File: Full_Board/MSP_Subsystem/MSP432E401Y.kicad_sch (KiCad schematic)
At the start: 4 parts, among them J1-J2 Conn_01x10, J3-J4 Conn_01x10, J5-J6 Conn_01x10, J7-J8 Conn_01x10

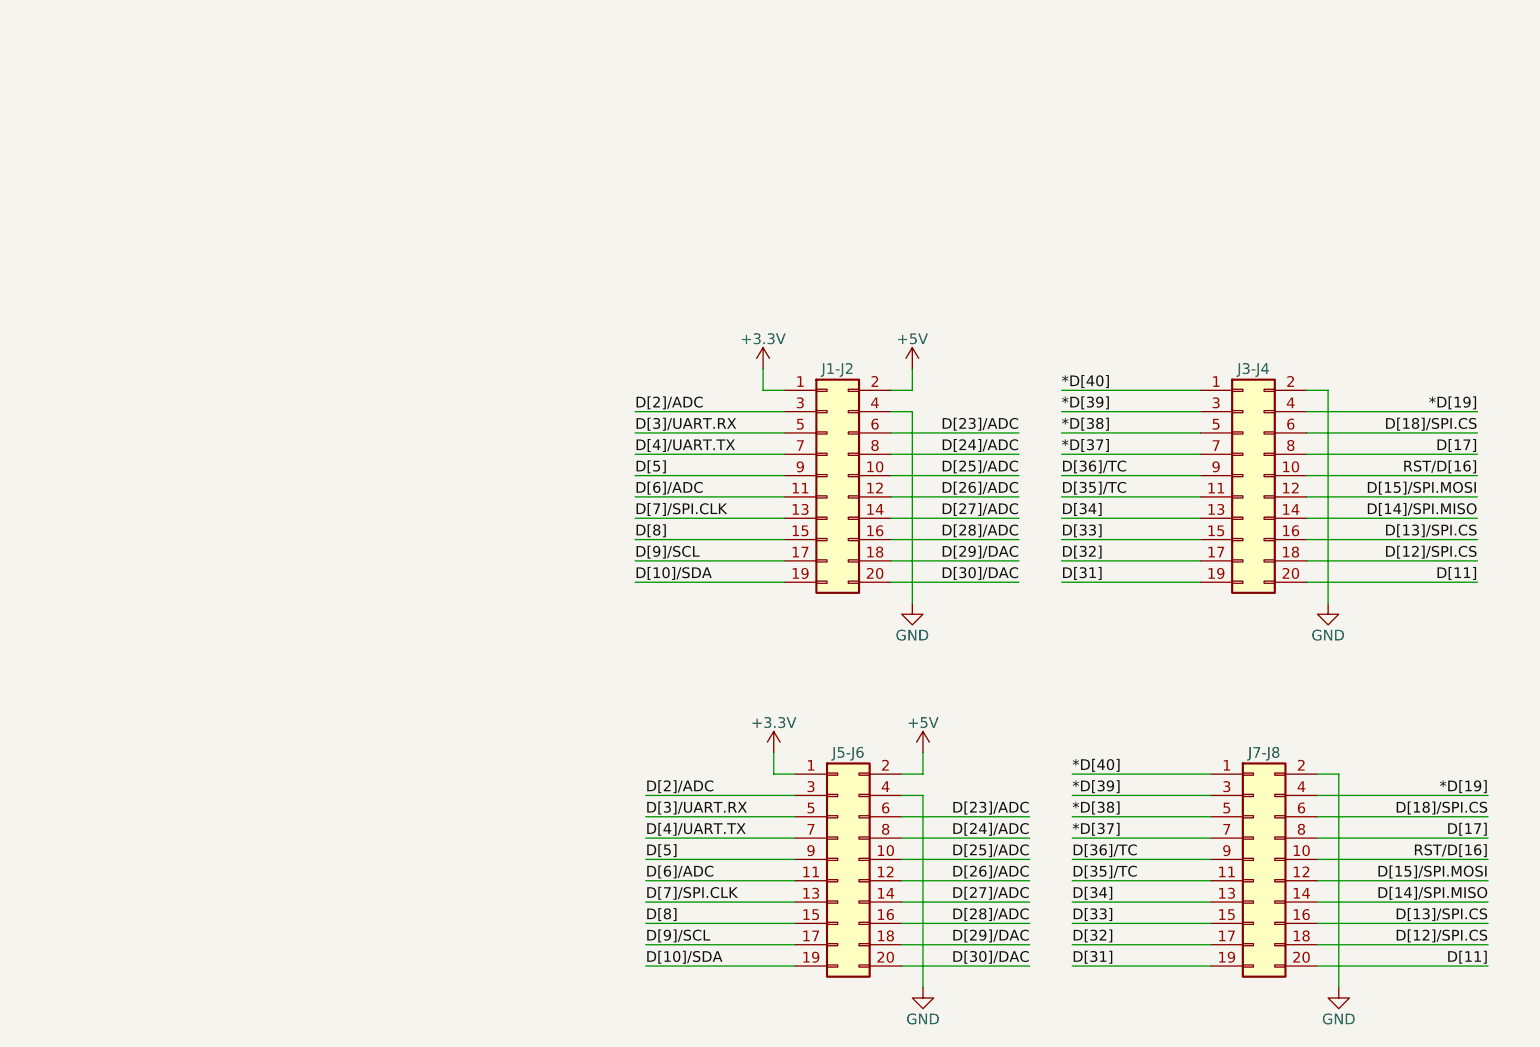
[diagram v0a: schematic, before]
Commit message: Finalize MSP432, stepper, and button subsheets
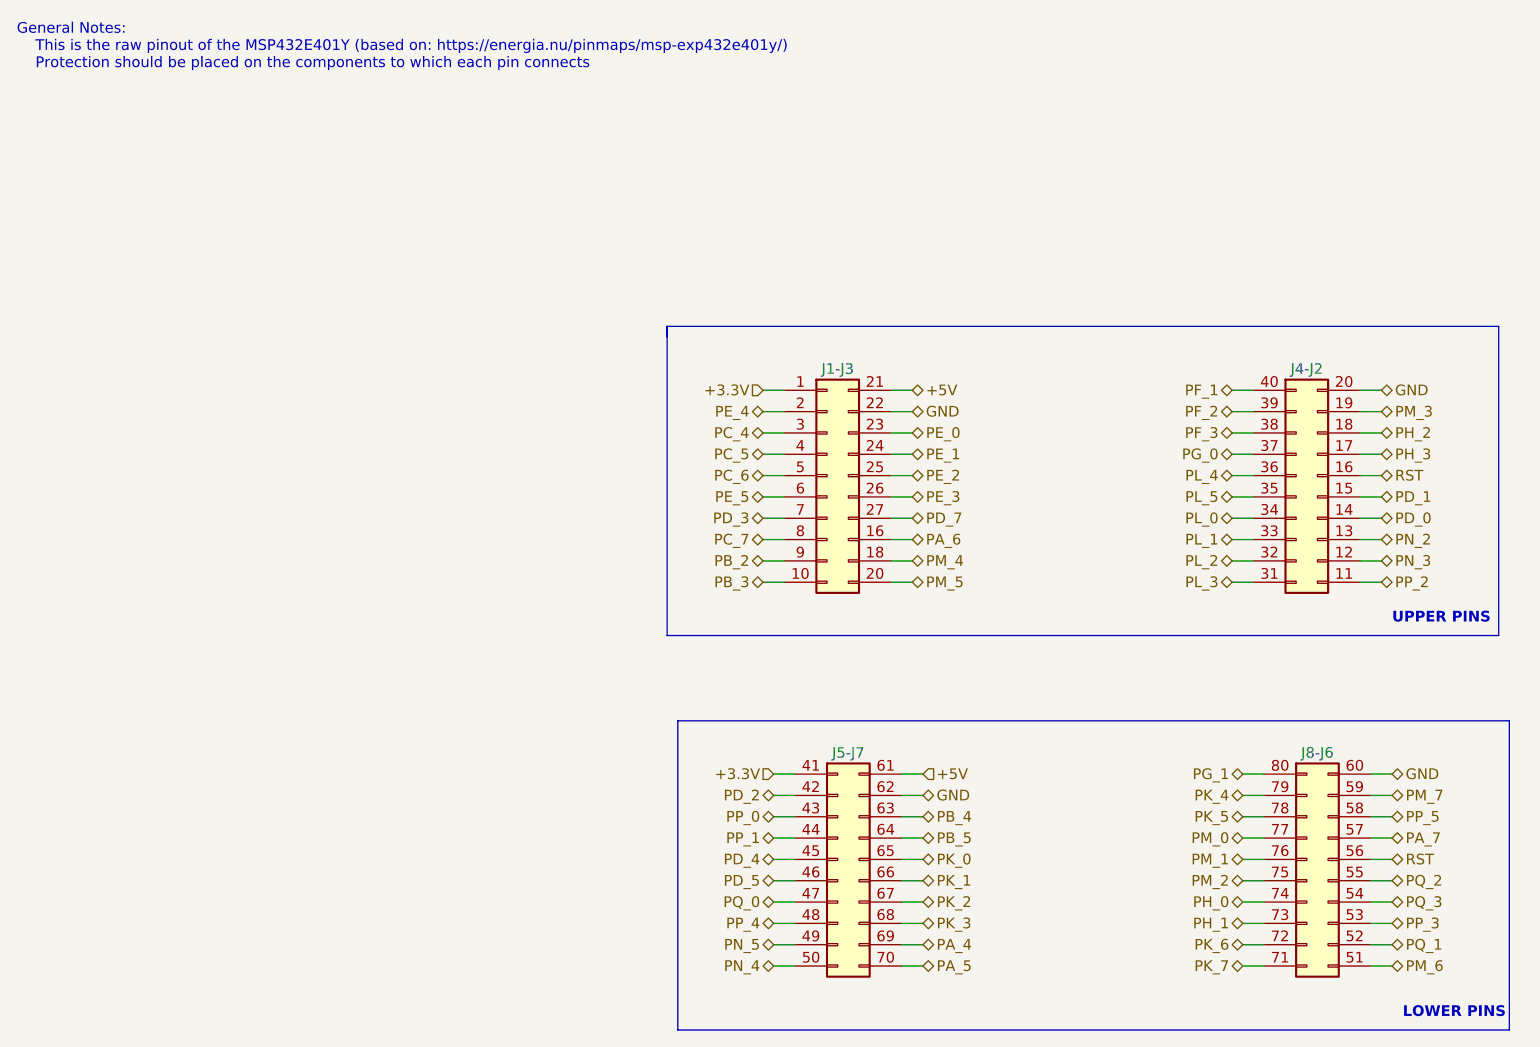
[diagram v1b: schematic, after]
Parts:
- removed J5-J6, J7-J8: Conn_01x10, Connector_PinSocket_2.54mm:PinSocket_2x10_P2.54mm_Vertical, symbol Connector_Generic:Conn_02x10_Odd_Even
- added J5-J7, J8-J6: Conn_01x10, Connector_PinSocket_2.54mm:PinSocket_2x10_P2.54mm_Vertical, symbol Connector_Generic:Conn_02x10_Odd_Even
- renumbered J1-J2 to J1-J3, J3-J4 to J4-J2
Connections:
- net D[11] is gone; now on net GND: J4-J2.20 (Pin_20)
- net +3.3V: now also J5-J7.41 (Pin_41)
- net +5V: now also J1-J3.21 (Pin_21), J5-J7.61 (Pin_61); no longer J1-J3.2 (Pin_2)
- net GND: now also J1-J3.22 (Pin_22), J5-J7.62 (Pin_62), J8-J6.60 (Pin_60); no longer J1-J3.4 (Pin_4), J4-J2.2 (Pin_2)
- removed net *D[19]: J4-J2.4 (Pin_4)
- removed net *D[37]: J4-J2.7 (Pin_7)
- removed net *D[38]: J4-J2.5 (Pin_5)
- removed net *D[39]: J4-J2.3 (Pin_3)
- removed net *D[40]: J4-J2.1 (Pin_1)
- removed net D[10]/SDA: J1-J3.19 (Pin_19)
- net D[12]/SPI.CS renamed PH_2
- net D[13]/SPI.CS renamed RST
- net RST: now also J8-J6.56 (Pin_56)
- net D[14]/SPI.MISO renamed PD_0
- net D[15]/SPI.MOSI renamed PN_3
- removed net D[17]: J4-J2.8 (Pin_8)
- removed net D[18]/SPI.CS: J4-J2.6 (Pin_6)
- net D[23]/ADC renamed PE_5
- net D[24]/ADC renamed PC_7
- net D[25]/ADC renamed PB_3
- removed net D[26]/ADC: J1-J3.12 (Pin_12)
- removed net D[27]/ADC: J1-J3.14 (Pin_14)
- net D[28]/ADC renamed PA_6
- net D[29]/DAC renamed PM_4
- net D[2]/ADC renamed PC_4
- net D[30]/DAC renamed PM_5
- net D[31] renamed PM_3
- net D[32] renamed PH_3
- net D[33] renamed PD_1
- net D[34] renamed PN_2
- net D[35]/TC renamed PP_2
- removed net D[36]/TC: J4-J2.9 (Pin_9)
- net D[3]/UART.RX renamed PC_6
- net D[4]/UART.TX renamed PD_3
- net D[5] renamed PB_2
- removed net D[6]/ADC: J1-J3.11 (Pin_11)
- removed net D[7]/SPI.CLK: J1-J3.13 (Pin_13)
- removed net D[8]: J1-J3.15 (Pin_15)
- removed net D[9]/SCL: J1-J3.17 (Pin_17)
- removed net RST/D[16]: J4-J2.10 (Pin_10)
- new net PA_4: J5-J7.69 (Pin_69)
- new net PA_5: J5-J7.70 (Pin_70)
- new net PA_7: J8-J6.57 (Pin_57)
- new net PB_4: J5-J7.63 (Pin_63)
- new net PB_5: J5-J7.64 (Pin_64)
- new net PC_5: J1-J3.4
- new net PD_2: J5-J7.42 (Pin_42)
- new net PD_4: J5-J7.45 (Pin_45)
- new net PD_5: J5-J7.46 (Pin_46)
- new net PD_7: J1-J3.27 (Pin_27)
- new net PE_0: J1-J3.23 (Pin_23)
- new net PE_1: J1-J3.24 (Pin_24)
- new net PE_2: J1-J3.25 (Pin_25)
- new net PE_3: J1-J3.26 (Pin_26)
- new net PE_4: J1-J3.2 (Pin_2)
- new net PF_1: J4-J2.40 (Pin_40)
- new net PF_2: J4-J2.39 (Pin_39)
- new net PF_3: J4-J2.38 (Pin_38)
- new net PG_0: J4-J2.37 (Pin_37)
- new net PG_1: J8-J6.80 (Pin_80)
- new net PH_0: J8-J6.74 (Pin_74)
- new net PH_1: J8-J6.73 (Pin_73)
- new net PK_0: J5-J7.65 (Pin_65)
- new net PK_1: J5-J7.66 (Pin_66)
- new net PK_2: J5-J7.67 (Pin_67)
- new net PK_3: J5-J7.68 (Pin_68)
- new net PK_4: J8-J6.79 (Pin_79)
- new net PK_5: J8-J6.78 (Pin_78)
- new net PK_6: J8-J6.72 (Pin_72)
- new net PK_7: J8-J6.71 (Pin_71)
- new net PL_0: J4-J2.34 (Pin_34)
- new net PL_1: J4-J2.33 (Pin_33)
- new net PL_2: J4-J2.32 (Pin_32)
- new net PL_3: J4-J2.31 (Pin_31)
- new net PL_4: J4-J2.36 (Pin_36)
- new net PL_5: J4-J2.35 (Pin_35)
- new net PM_0: J8-J6.77 (Pin_77)
- new net PM_1: J8-J6.76 (Pin_76)
- new net PM_2: J8-J6.75 (Pin_75)
- new net PM_6: J8-J6.51 (Pin_51)
- new net PM_7: J8-J6.59 (Pin_59)
- new net PN_4: J5-J7.50 (Pin_50)
- new net PN_5: J5-J7.49 (Pin_49)
- new net PP_0: J5-J7.43 (Pin_43)
- new net PP_1: J5-J7.44 (Pin_44)
- new net PP_3: J8-J6.53 (Pin_53)
- new net PP_4: J5-J7.48 (Pin_48)
- new net PP_5: J8-J6.58 (Pin_58)
- new net PQ_0: J5-J7.47 (Pin_47)
- new net PQ_1: J8-J6.52 (Pin_52)
- new net PQ_2: J8-J6.55 (Pin_55)
- new net PQ_3: J8-J6.54 (Pin_54)
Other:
- note added: "General Notes: This is the raw pinout of the MSP432E401Y (based on: https://energia.nu/pinmaps/msp-exp432e401y/) Protection should be placed on the components to which each pin connects"
- note added: "LOWER PINS"
- note added: "UPPER PINS"
- moved on the sheet: J4-J2
